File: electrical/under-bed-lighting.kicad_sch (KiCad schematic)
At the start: 21 parts, among them J1 PJ-002AH, J2 PZ254V-11-03P, Q1 AO3401A, U1 ESP32-C3 Super Mini, U2 LMR51606YFDBVR, U3 SN74LVC08ADR

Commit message: working on layout
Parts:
- J2: value PZ254V-11-03P -> 0705430002; JLCPCB PN C2937625 -> C504828; now fitted
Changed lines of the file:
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@@
 		(in_bom yes)
 		(on_board yes)
-		(dnp yes)
+		(dnp no)
 		(property "Reference" "J2"
 			(at 106.68 107.95 0)
@@
 			)
 		)
-		(property "Value" "PZ254V-11-03P"
+		(property "Value" "0705430002"
 			(at 114.3 123.19 0)
 			(effects
@@
 			)
 		)
-		(property "Datasheet" "https://jlcpcb.com/api/file/downloadByFileSystemAccessId/8588954567287443456"
+		(property "Datasheet" "https://www.molex.com/pdm_docs/sd/705430001_sd.pdf"
 			(at 106.68 116.84 0)
 			(effects
@@
 			)
 		)
-		(property "JLCPCB PN" "C2937625"
+		(property "JLCPCB PN" "C504828"
 			(at 106.68 116.84 0)
 			(effects
@@
 			(at 106.68 116.84 0)
 			(effects
-				(font
-					(size 1.27 1.27)
-				)
-				(hide yes)
-			)
-		)
-		(property "FT Origin" ""
-			(at 106.68 116.84 0)
-			(effects
-				(font
-					(size 1.27 1.27)
-				)
-				(hide yes)
-			)
-		)
-		(property "FT Position Offset" ""
-			(at 106.68 116.84 0)
-			(effects
-				(font
-					(size 1.27 1.27)
-				)
-				(hide yes)
-			)
-		)
-		(property "FT Rotation Offset" ""
-			(at 106.68 116.84 0)
-			(effects

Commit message: Layout complete
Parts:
- added H1, H2, H3, H4: MountingHole_Pad, MountingHole:MountingHole_2mm, symbol Mechanical:MountingHole_Pad
- J1: FT Rotation Offset (none) -> 180
- J2: JLCPCB PN C504828 -> C2937625
- L1: value 74404064180 -> SWPA6045S180MT; symbol !Inductor-Power:74404064180 -> !Inductor-Power:SWPA6045S180MT; JLCPCB PN C1332431 -> C96954
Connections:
- net LED2: now also U1.3 (GPIO7); no longer U1.4 (GPIO8)
- no-connect marks 4 -> 8
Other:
- title: (none) -> Under-bed Lighting Controller

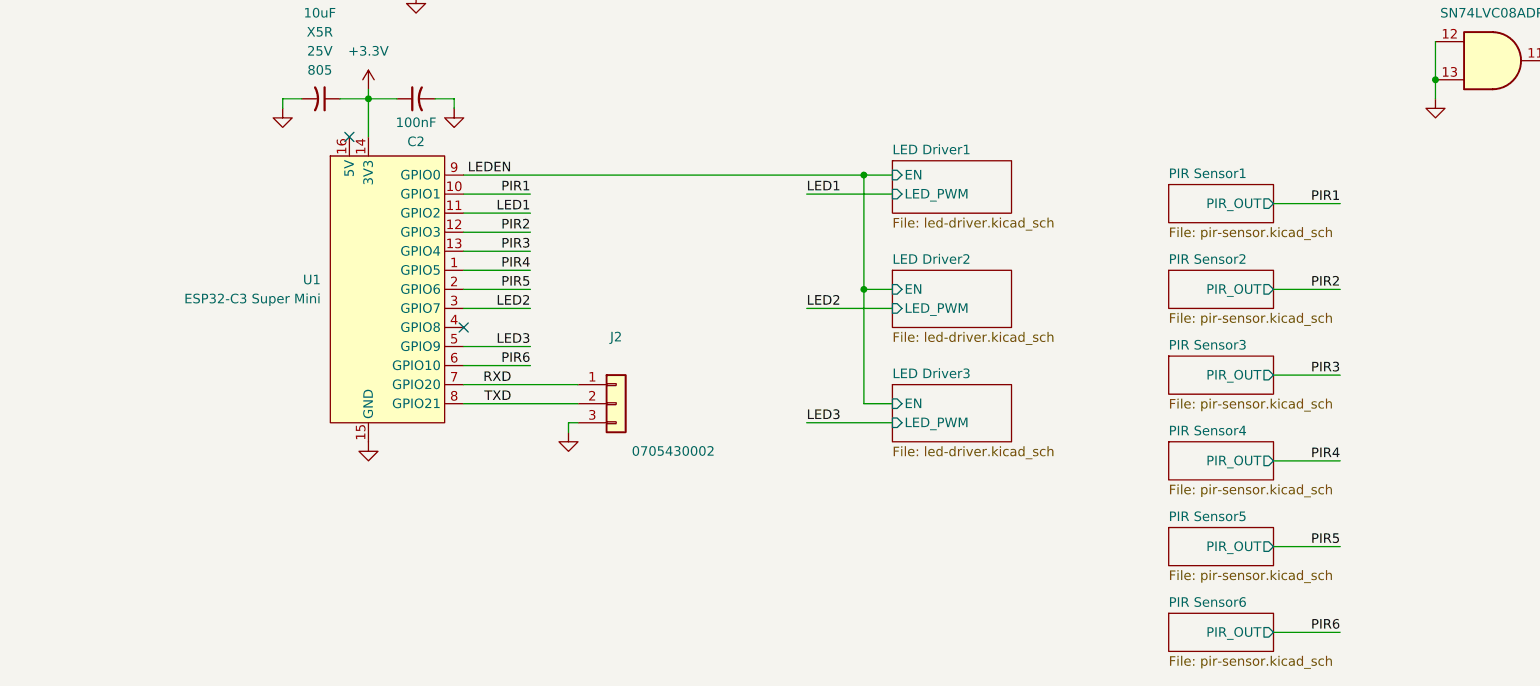
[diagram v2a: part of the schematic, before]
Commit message: Migration to ESP32-C3-OLED in process
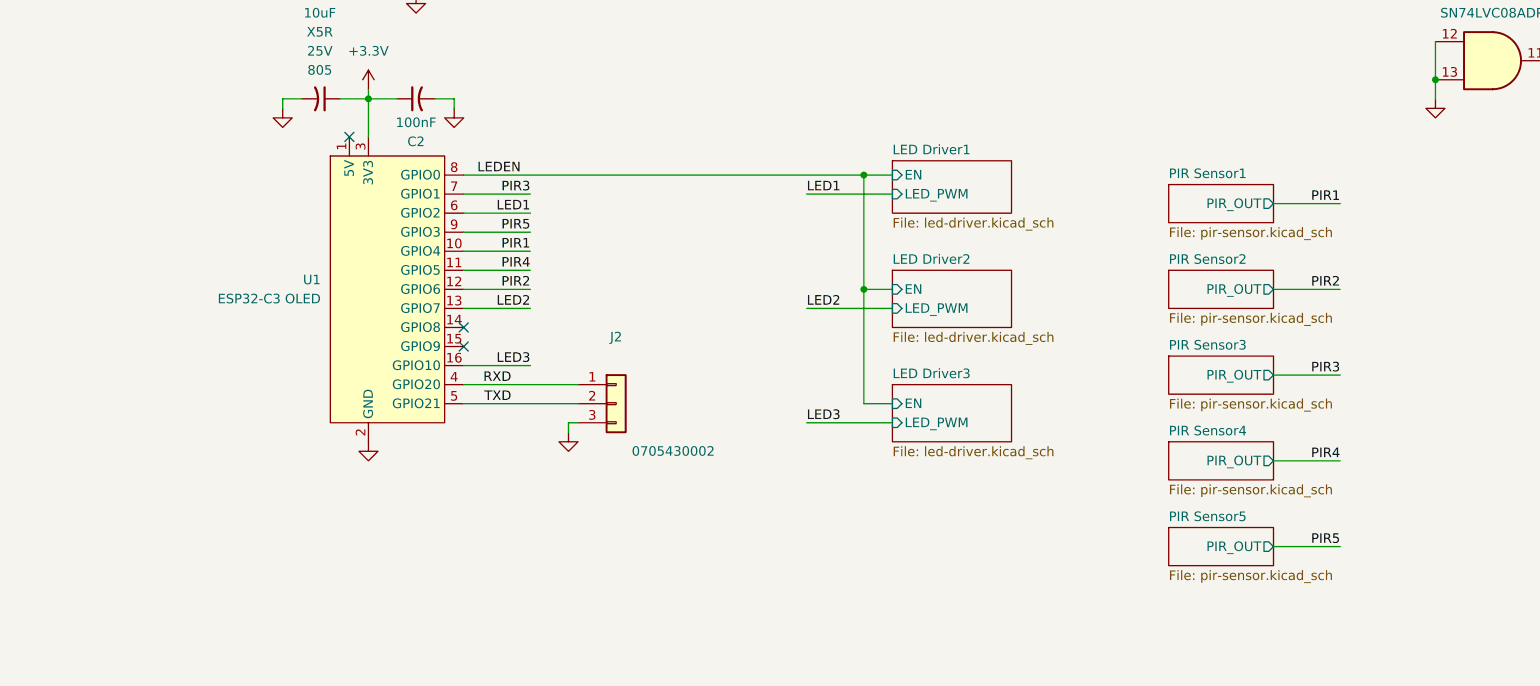
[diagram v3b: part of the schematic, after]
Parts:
- U1: value ESP32-C3 Super Mini -> ESP32-C3 OLED; symbol !RF Modules:ESP32-C3_Super_Mini -> !RF Modules:ESP32-C3 OLED
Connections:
- net PIR6 is gone; now on net LED1: U1.6 (GPIO2)
- net +3.3V: now also U1.3 (3V3); no longer U1.14 (3V3)
- net GND: now also U1.2 (GND); no longer U1.15 (GND)
- net LED1: no longer U1.11 (GPIO2)
- net LED2: now also U1.13 (GPIO7); no longer U1.3 (GPIO7)
- net LED3: now also U1.16 (GPIO10); no longer U1.5 (GPIO9)
- net LEDEN: now also U1.8 (GPIO0); no longer U1.9 (GPIO0)
- net PIR3: now also U1.7 (GPIO1); no longer U1.13 (GPIO4)
- net PIR4: now also U1.11 (GPIO5); no longer U1.1 (GPIO5)
- net PIR5: now also U1.9 (GPIO3); no longer U1.2 (GPIO6)
- net RXD: now also U1.4 (GPIO20); no longer U1.7 (GPIO20)
- net TXD: now also U1.5 (GPIO21); no longer U1.8 (GPIO21)
- no-connect marks 8 -> 9
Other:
- removed sheet PIR Sensor6
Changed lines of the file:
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@@
 	)
 	(no_connect
+		(at 86.36 109.22)
+	)
+	(no_connect
 		(at 276.86 46.99)
 	)
@@
 	(wire
 		(pts
-			(xy 86.36 114.3) (xy 101.6 114.3)
+			(xy 86.36 99.06) (xy 95.25 99.06)
 		)
 		(stroke
@@
 	(wire
 		(pts
-			(xy 86.36 99.06) (xy 95.25 99.06)
+			(xy 85.09 38.1) (xy 91.44 38.1)
 		)
 		(stroke
@@
 	(wire
 		(pts
-			(xy 85.09 38.1) (xy 91.44 38.1)
+			(xy 119.38 38.1) (xy 129.54 38.1)
 		)
 		(stroke
@@
 	(wire
 		(pts
-			(xy 119.38 38.1) (xy 129.54 38.1)
+			(xy 86.36 114.3) (xy 101.6 114.3)
 		)
 		(stroke
@@
 	(wire
 		(pts
-			(xy 86.36 109.22) (xy 95.25 109.22)
-		)
-		(stroke
-			(width 0)
-			(type default)
-		)
-	)
-	(wire
-		(pts
 			(xy 62.23 76.2) (xy 62.23 77.47)
 		)
@@
 	(wire
 		(pts
-			(xy 91.44 53.34) (xy 91.44 50.8)
+			(xy 86.36 111.76) (xy 95.25 111.76)
 		)
 		(stroke
@@
 	(wire
 		(pts
-			(xy 229.87 25.4) (xy 229.87 26.67)
+			(xy 91.44 53.34) (xy 91.44 50.8)
 		)
 		(stroke
@@
 	(wire
 		(pts
-			(xy 194.31 113.03) (xy 203.2 113.03)
+			(xy 229.87 25.4) (xy 229.87 26.67)
 		)
 		(stroke
@@
 	(wire
 		(pts
-			(xy 86.36 88.9) (xy 95.25 88.9)
+			(xy 194.31 113.03) (xy 203.2 113.03)
 		)
 		(stroke
@@
 	(wire
 		(pts
-			(xy 73.66 76.2) (xy 77.47 76.2)
+			(xy 86.36 88.9) (xy 95.25 88.9)
 		)
 		(stroke
@@
 	(wire
 		(pts
-			(xy 64.77 76.2) (xy 62.23 76.2)
+			(xy 73.66 76.2) (xy 77.47 76.2)
 		)
 		(stroke
@@
 	(wire
 		(pts
-			(xy 100.33 119.38) (xy 100.33 120.65)
+			(xy 64.77 76.2) (xy 62.23 76.2)
 		)
 		(stroke
@@
 	(wire
 		(pts
-			(xy 80.01 52.07) (xy 80.01 53.34)
+			(xy 100.33 119.38) (xy 100.33 120.65)
 		)
 		(stroke
@@
 	(wire
 		(pts
-			(xy 194.31 147.32) (xy 203.2 147.32)
+			(xy 80.01 52.07) (xy 80.01 53.34)
 		)
 		(stroke
@@
 	(wire
 		(pts
-			(xy 86.36 111.76) (xy 95.25 111.76)
-		)
-		(stroke
-			(width 0)
-			(type default)
-		)
-	)
-	(wire
-		(pts
 			(xy 73.66 74.93) (xy 73.66 76.2)
 		)
@@
 	)
 	(label "LED3"
-		(at 95.25 109.22 180)
+		(at 95.25 111.76 180)
 		(effects
 			(font
@@
 		)
 	)
-	(label "PIR1"
-		(at 95.25 88.9 180)
+	(label "PIR5"
+		(at 95.25 93.98 180)
 		(effects
 			(font
@@
 		)
 	)
-	(label "PIR2"
-		(at 95.25 93.98 180)
-		(effects
-			(font
-				(size 1.27 1.27)
-			)
-			(justify right bottom)
-		)
-	)
 	(label "PIR5"
 		(at 203.2 135.89 180)
@@
 		)
 	)
-	(label "PIR6"
-		(at 203.2 147.32 180)
-		(effects
-			(font
-				(size 1.27 1.27)
-			)
-			(justify right bottom)
-		)
-	)
 	(label "LED3"
 		(at 132.08 119.38 0)
@@
 		)
 	)
-	(label "PIR3"
+	(label "PIR1"
 		(at 95.25 96.52 180)
 		(effects
@@
 	)
 	(label "LEDEN"
-		(at 92.71 86.36 180)
+		(at 93.98 86.36 180)
 		(effects
 			(font
@@
 		)
 	)
-	(label "PIR6"
-		(at 95.25 111.76 180)
+	(label "PIR4"
+		(at 203.2 124.46 180)
 		(effects
 			(font
@@
 		)
 	)
-	(label "PIR4"
-		(at 203.2 124.46 180)
+	(label "PIR3"
+		(at 95.25 88.9 180)
 		(effects
 			(font
@@
 		)
 	)
-	(label "PIR5"
+	(label "PIR2"
 		(at 95.25 101.6 180)
 		(effects
@@
 	)
 	(symbol
-		(lib_id "!RF Modules:ESP32-C3_Super_Mini")
+		(lib_id "!RF Modules:ESP32-C3 OLED")
 		(at 76.2 101.6 0)
 		(unit 1)
@@
 			)
 		)
-		(property "Value" "ESP32-C3 Super Mini"
+		(property "Value" "ESP32-C3 OLED"
 			(at 67.31 102.8699 0)
 			(effects
@@
 			)
 		)
-		(property "Datasheet" "https://dl.artronshop.co.th/ESP32-C3%20SuperMini%20datasheet.pdf"
+		(property "Datasheet" "https://www.espboards.dev/esp32/esp32-c3-oled-042/"
 			(at 76.2 101.6 0)
 			(effects
@@
 				)
 			)
-		)
-	)
-	(sheet
-		(at 180.34 144.78)
-		(size 13.97 5.08)
-		(exclude_from_sim no)
-		(in_bom yes)
-		(on_board yes)
-		(dnp no)
-		(fields_autoplaced yes)
-		(stroke
-			(width 0.1524)
-			(type solid)
-		)
-		(fill
-			(color 0 0 0 0.0000)
-		)
-		(property "Sheetname" "PIR Sensor6"
-			(at 180.34 144.0684 0)
-			(effects
-				(font
-					(size 1.27 1.27)
-				)
-				(justify left bottom)
-			)
-		)
-		(property "Sheetfile" "pir-sensor.kicad_sch"
-			(at 180.34 150.4446 0)
-			(effects
-				(font
-					(size 1.27 1.27)
-				)
-				(justify left top)
-			)
-		)
-		(pin "PIR_OUT" output
-			(at 194.31 147.32 0)
-			(effects
-				(font
-					(size 1.27 1.27)
-				)
-				(justify right)
-			)
-		)
-		(instances
-			(project "under-bed-lighting"
-				(path "/539bcff6-33eb-4388-b0b8-7341b324bbe7"
-					(page "10")
-				)
-			)

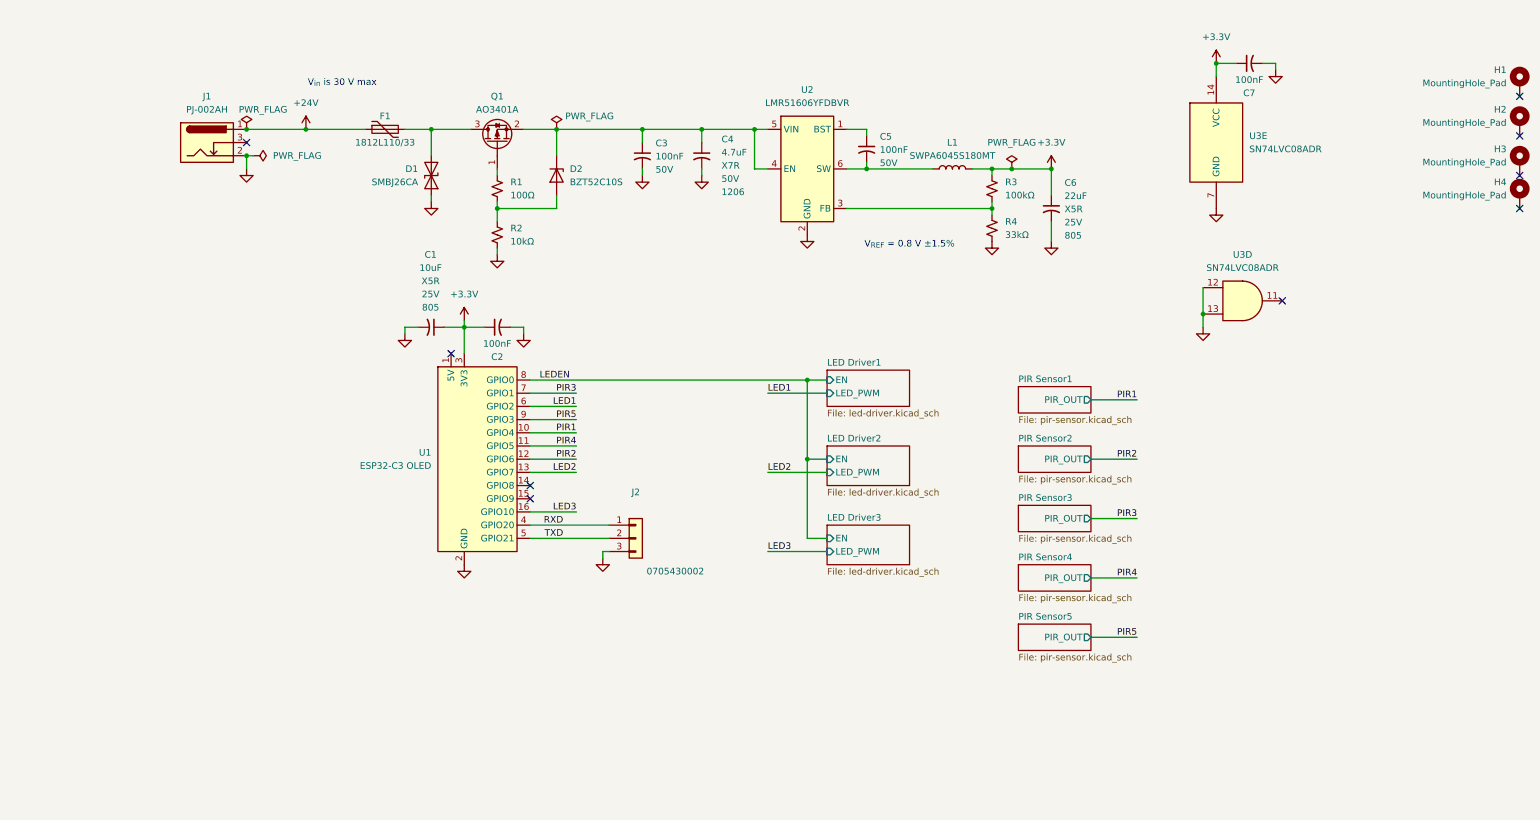
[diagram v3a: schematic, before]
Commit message: Finished and submitted to JLCPCB
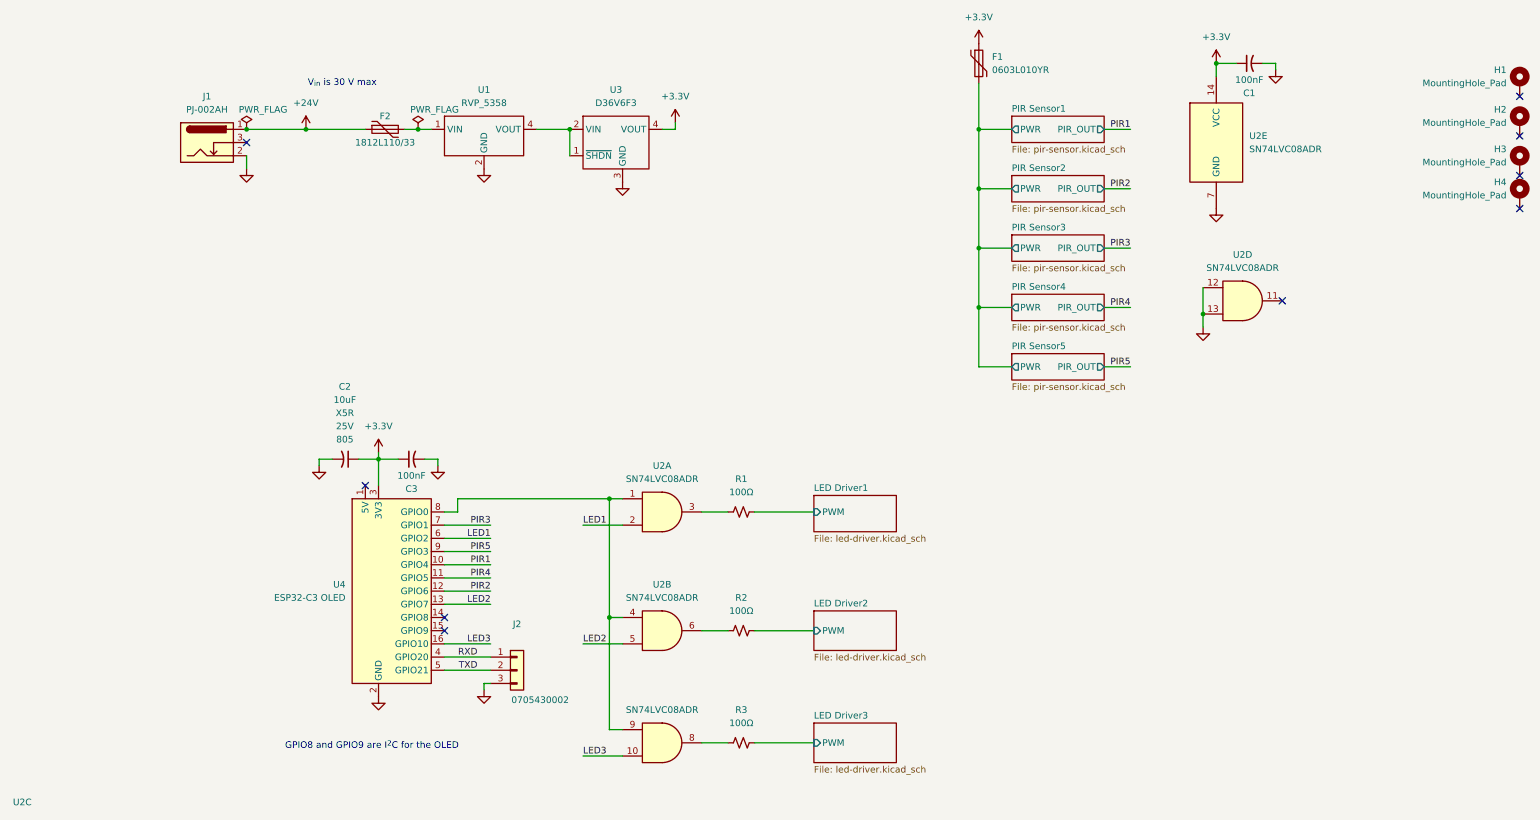
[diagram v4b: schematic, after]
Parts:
- removed C3, C5: 100nF, Capacitor_SMD:C_0603_1608Metric, symbol !Capacitor-0603:100nF_X7R_50V
- removed C4: 4.7uF, Capacitor_SMD:C_1206_3216Metric, symbol !Capacitor-1206:4.7uF_X7R_50V
- removed C6: 22uF, Capacitor_SMD:C_0805_2012Metric, symbol !Capacitor-0805:22uF_X5R_25V
- removed D1: SMBJ26CA, Diode_SMD:D_SMB, symbol !Circuit Protection-ESD+TVS:SMBJ26A
- removed D2: BZT52C10S, Diode_SMD:D_SOD-323, symbol !Diode-Zener:BZT52C10S
- removed L1: SWPA6045S180MT, !Inductors:WE-LQS_6045, symbol !Inductor-Power:SWPA6045S180MT
- removed Q1: AO3401A, Package_TO_SOT_SMD:TSOT-23, symbol !MOSFET:AO3401A
- removed R2: 10kΩ, Resistor_SMD:R_0603_1608Metric, symbol !Resistor-0603:10kΩ
- removed R3: 100kΩ, Resistor_SMD:R_0603_1608Metric, symbol !Resistor-0603:100kΩ
- removed R4: 33kΩ, Resistor_SMD:R_0603_1608Metric, symbol !Resistor-0603:33kΩ
- removed U2: LMR51606YFDBVR, Package_TO_SOT_SMD:SOT-23-6, symbol !Power Management:LMR51606YFDBVR
- added F1: 0603L010YR, Fuse:Fuse_0603_1608Metric, symbol !Circuit Protection-Resettable Fuse:0603L010YR
- added R2, R3: 100Ω, Resistor_SMD:R_0603_1608Metric, symbol !Resistor-0603:100Ω
- added U1: RVP_5358, !Pololu:RVP_5358, symbol !Pololu:RVP_5358
- added unit 1 of U2
- added unit 3 of U2
- added unit 2 of U2
- added U3: D36V6F3, !Pololu:D36V6x, symbol !Pololu:D36V6F3
- renumbered C7 to C1, C1 to C2, C2 to C3, F1 to F2, U3 to U2, U1 to U4
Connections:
- net +3.3V: now also F1.1, U3.4 (VOUT)
- net GND: now also U1.2 (GND), U1.3 (GND), U3.3 (GND)
- net LED1: now also U2.2
- net LED2: now also U2.5
- net LED3: now also U2.10
- net at R1.1: now also U2.3
- net LED Driver1/PWM: now reaches R1.2
- net at F2.2: now also U1.1 (VIN)
- net LEDEN: no longer names the net of U4.8 (GPIO0)
- net LEDEN: now also U2.1, U2.4, U2.9
- new net: R3.1, U2.8
- new net: U1.4 (VOUT), U3.1 (~{SHDN}), U3.2 (VIN)
- new net: R2.1, U2.6
- new net LED Driver2/PWM: R2.2
- new net LED Driver3/PWM: R3.2
- new net PIR Sensor1/PWR: F1.2
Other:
- sheet LED Driver1 ports: added PWM; removed EN, LED_PWM
- sheet LED Driver2 ports: added PWM; removed EN, LED_PWM
- sheet LED Driver3 ports: added PWM; removed EN, LED_PWM
- sheet PIR Sensor1 ports: added PWR; removed none
- sheet PIR Sensor2 ports: added PWR; removed none
- sheet PIR Sensor3 ports: added PWR; removed none
- sheet PIR Sensor4 ports: added PWR; removed none
- sheet PIR Sensor5 ports: added PWR; removed none
- note added: "GPIO8 and GPIO9 are I^{2}C for the OLED"
- note removed: "V_{REF} = 0.8 V ±1.5%"
- moved on the sheet: C2, C3, J2, U4
